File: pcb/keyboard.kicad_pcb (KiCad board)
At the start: 2 copper layers, 72.2 x 98 mm, 23 parts, among them SW1 SW_Push, SW2 SW_Push, SW3 RotaryEncoder_Switch, SW3 SW_Push, SW4 SW_Push, SW5 SW_Push, SW6 SW_Push, SW7 SW_Push, SW8 SW_Push, SW9 SW_Push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

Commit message: delete the current pcb situation - too many changes were made to the schem
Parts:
- removed D1, D2, D3, D4, D5, D6, D7, D8, D9: 1N4148, Diode_THT:D_DO-35_SOD27_P7.62mm_Horizontal
- removed D10, D11: SK6812MINI-E, footprints:SK6812MINI-E_fixed
- removed SW1, SW2, SW3, SW4, SW5, SW6, SW7, SW8, SW9: SW_Push, Button_Switch_Keyboard:SW_Cherry_MX_1.00u_PCB
- removed SW3: RotaryEncoder_Switch, Rotary_Encoder:RotaryEncoder_Alps_EC11E-Switch_Vertical_H20mm
- removed U1: MOUDLE-SEEEDUINO-XIAO, footprints:XIAO-Generic-Hybrid-14P-2.54-21X17.8MM
- removed U2: ER_OLEDM0.91_1x-I2C, Display:ER_OLEDM0.91_1x-I2C
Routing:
- net Row 2: track 154.9 -> 0.00 mm
- net Row 1: track 133.4 -> 0.00 mm
- net Row 0: track 113.0 -> 0.00 mm
- net Column 2: track 104.2 -> 0.00 mm
- net GND: track 96.8 -> 0.00 mm, vias 1 -> 0
- net Column 1: track 87.1 -> 0.00 mm
- net Column 0: track 81.6 -> 0.00 mm
- net VCC: track 43.9 -> 0.00 mm
- net ROT A: track 26.5 -> 0.00 mm
- net ROT B: track 25.5 -> 0.00 mm
- net SCL: track 24.5 -> 0.00 mm
- net SDA: track 24.5 -> 0.00 mm
- net (no net): track 22.6 -> 0.00 mm
- net Net-(D7-A): track 5.95 -> 0.00 mm
- net Net-(D4-A): track 5.91 -> 0.00 mm
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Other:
- board outline removed

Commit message: align switches, board and screen on the pcb
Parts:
- added D1: 1N4148, Diode_THT:D_DO-35_SOD27_P7.62mm_Horizontal, F.Cu at (117.3, 93.5)
- added D10: SK6812MINI-E, footprints:SK6812MINI-E_fixed, F.Cu at (175.5, 70.5)
- added D11: SK6812MINI-E, footprints:SK6812MINI-E_fixed, F.Cu at (216.0, 70.5)
- added D2: 1N4148, Diode_THT:D_DO-35_SOD27_P7.62mm_Horizontal, F.Cu at (117.3, 97.0)
- added D3: 1N4148, Diode_THT:D_DO-35_SOD27_P7.62mm_Horizontal, F.Cu at (117.3, 100.5)
- added D4: 1N4148, Diode_THT:D_DO-35_SOD27_P7.62mm_Horizontal, F.Cu at (117.3, 104.1)
- added D5: 1N4148, Diode_THT:D_DO-35_SOD27_P7.62mm_Horizontal, F.Cu at (117.3, 107.7)
- added D6: 1N4148, Diode_THT:D_DO-35_SOD27_P7.62mm_Horizontal, F.Cu at (117.3, 111.2)
- added D7: 1N4148, Diode_THT:D_DO-35_SOD27_P7.62mm_Horizontal, F.Cu at (117.3, 114.8)
- added D8: 1N4148, Diode_THT:D_DO-35_SOD27_P7.62mm_Horizontal, F.Cu at (117.3, 118.3)
- added D9: 1N4148, Diode_THT:D_DO-35_SOD27_P7.62mm_Horizontal, F.Cu at (117.3, 121.8)
- added SW1: SW_Push, Button_Switch_Keyboard:SW_Cherry_MX_1.00u_PCB, F.Cu at (178.3, 77.7)
- added SW2: SW_Push, Button_Switch_Keyboard:SW_Cherry_MX_1.00u_PCB, F.Cu at (198.0, 77.7)
- added SW3: RotaryEncoder_Switch, Rotary_Encoder:RotaryEncoder_Alps_EC11E-Switch_Vertical_H20mm, F.Cu at (208.2, 79.8)
- added SW4: SW_Push, Button_Switch_Keyboard:SW_Cherry_MX_1.00u_PCB, F.Cu at (178.3, 97.4)
- added SW5: SW_Push, Button_Switch_Keyboard:SW_Cherry_MX_1.00u_PCB, F.Cu at (198.0, 97.4)
- added SW6: SW_Push, Button_Switch_Keyboard:SW_Cherry_MX_1.00u_PCB, F.Cu at (217.7, 97.4)
- added SW7: SW_Push, Button_Switch_Keyboard:SW_Cherry_MX_1.00u_PCB, F.Cu at (178.3, 117.1)
- added SW8: SW_Push, Button_Switch_Keyboard:SW_Cherry_MX_1.00u_PCB, F.Cu at (217.7, 117.1)
- added SW9: SW_Push, Button_Switch_Keyboard:SW_Cherry_MX_1.00u_PCB, F.Cu at (198.0, 117.1)
- added U1: MODULE-SEEEDUINO-XIAO-RP2040, footprints:XIAO-Generic-Hybrid-14P-2.54-21X17.8MM, F.Cu at (175.4, 56.2)
- added U2: ER_OLEDM0.91_1x-I2C, Display:ER_OLEDM0.91_1x-I2C, F.Cu at (189.5, 59.3)
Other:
- board outline added: 70 x 95 mm

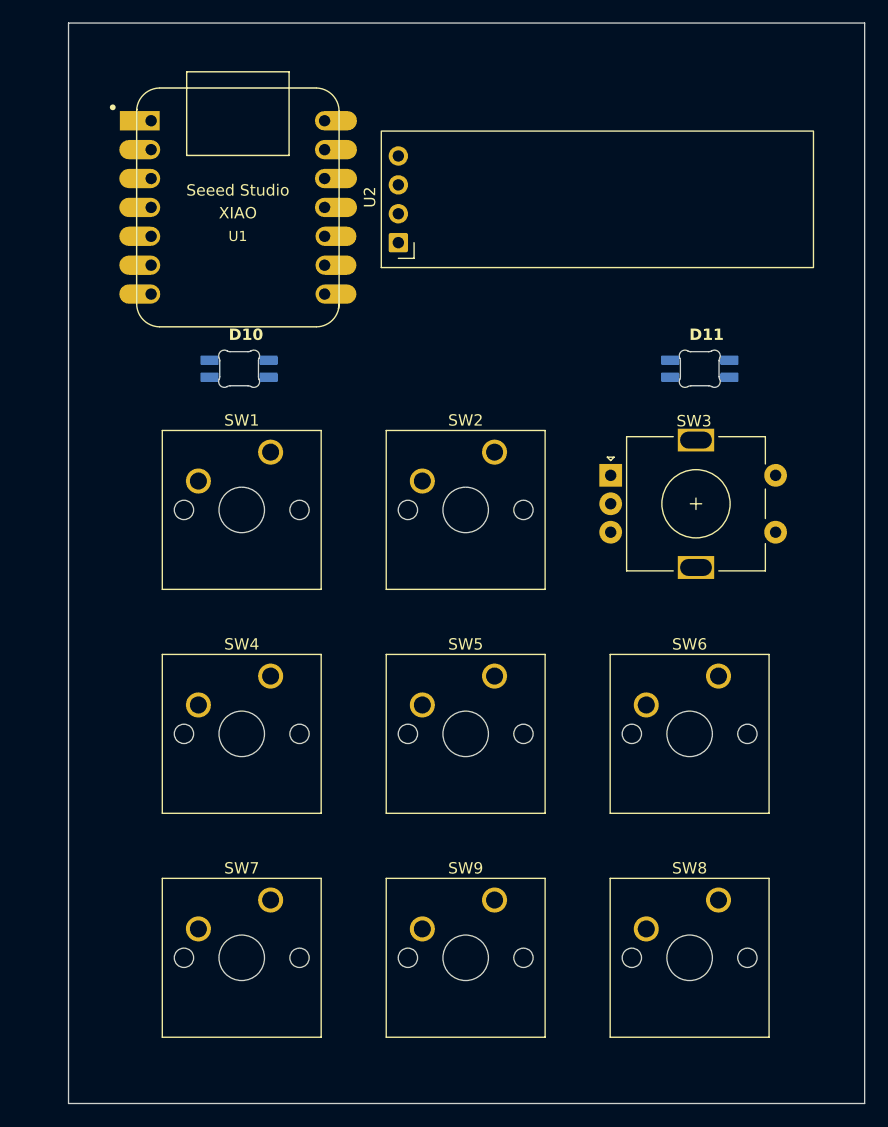
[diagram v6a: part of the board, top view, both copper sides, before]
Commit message: make the board smaller, add third rgb
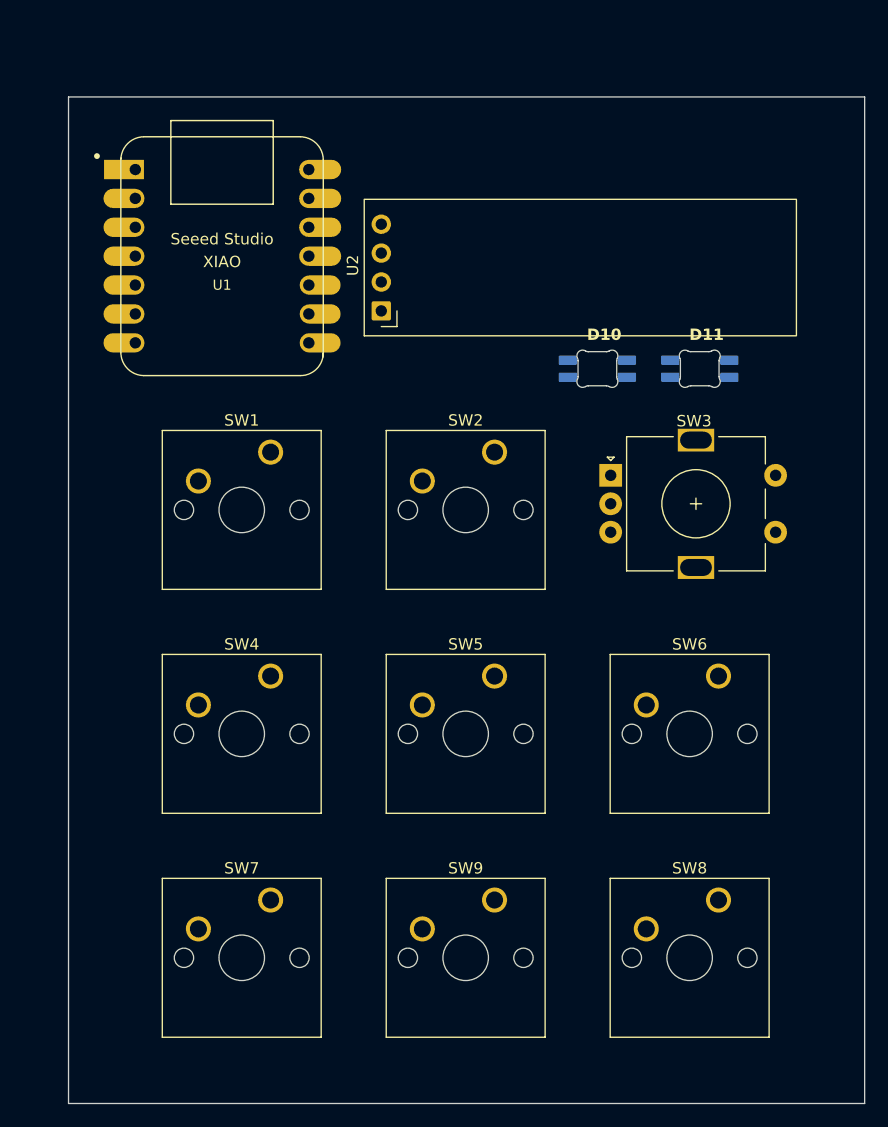
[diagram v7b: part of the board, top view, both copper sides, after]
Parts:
- moved D10 31.5 mm to (207.0, 70.5)
- moved U2 6.18 mm to (188.0, 65.3)
- moved U1 4.51 mm to (174.0, 60.5)
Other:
- board size 70 x 95 mm -> 70 x 88.5 mm
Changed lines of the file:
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@@
 	(footprint "footprints:SK6812MINI-E_fixed"
 		(layer "F.Cu")
-		(at 175.5 70.5)
+		(at 207 70.5)
 		(descr "Add-on for regular MX-footprints with SK6812 MINI-E")
 		(tags "cherry MX SK6812 Mini-E rearmount rear mount led rgb backlight")
@@
 	(footprint "Display:ER_OLEDM0.91_1x-I2C"
 		(layer "F.Cu")
-		(at 189.5 59.31 90)
+		(at 188 65.31 90)
 		(descr "SSD1306 OLED module, 0.91 inch, 128x32, I2C (https://www.buydisplay.com/download/manual/ER-OLEDM0.91-1_Datasheet.pdf)")
 		(tags "EastRising")
@@
 	(footprint "footprints:XIAO-Generic-Hybrid-14P-2.54-21X17.8MM"
 		(layer "F.Cu")
-		(at 175.3895 56.212015)
+		(at 174 60.5)
 		(property "Reference" "U1"
 			(at 0 2.54 0)
@@
 	)
 	(gr_rect
-		(start 160.5 40)
+		(start 160.5 46.5)
 		(end 230.5 135)
 		(stroke

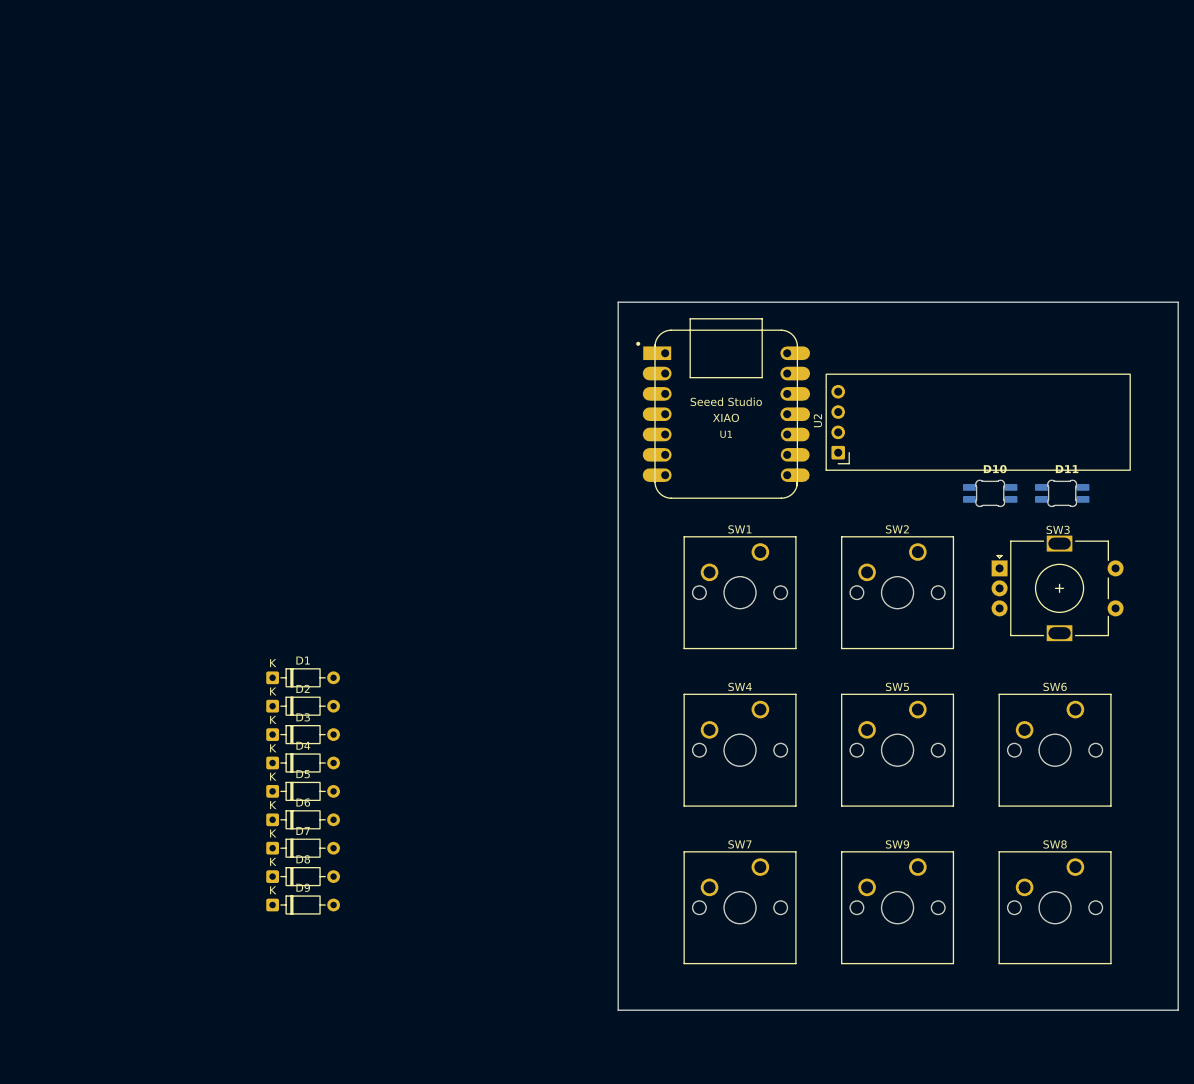
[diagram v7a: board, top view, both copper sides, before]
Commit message: align diodes
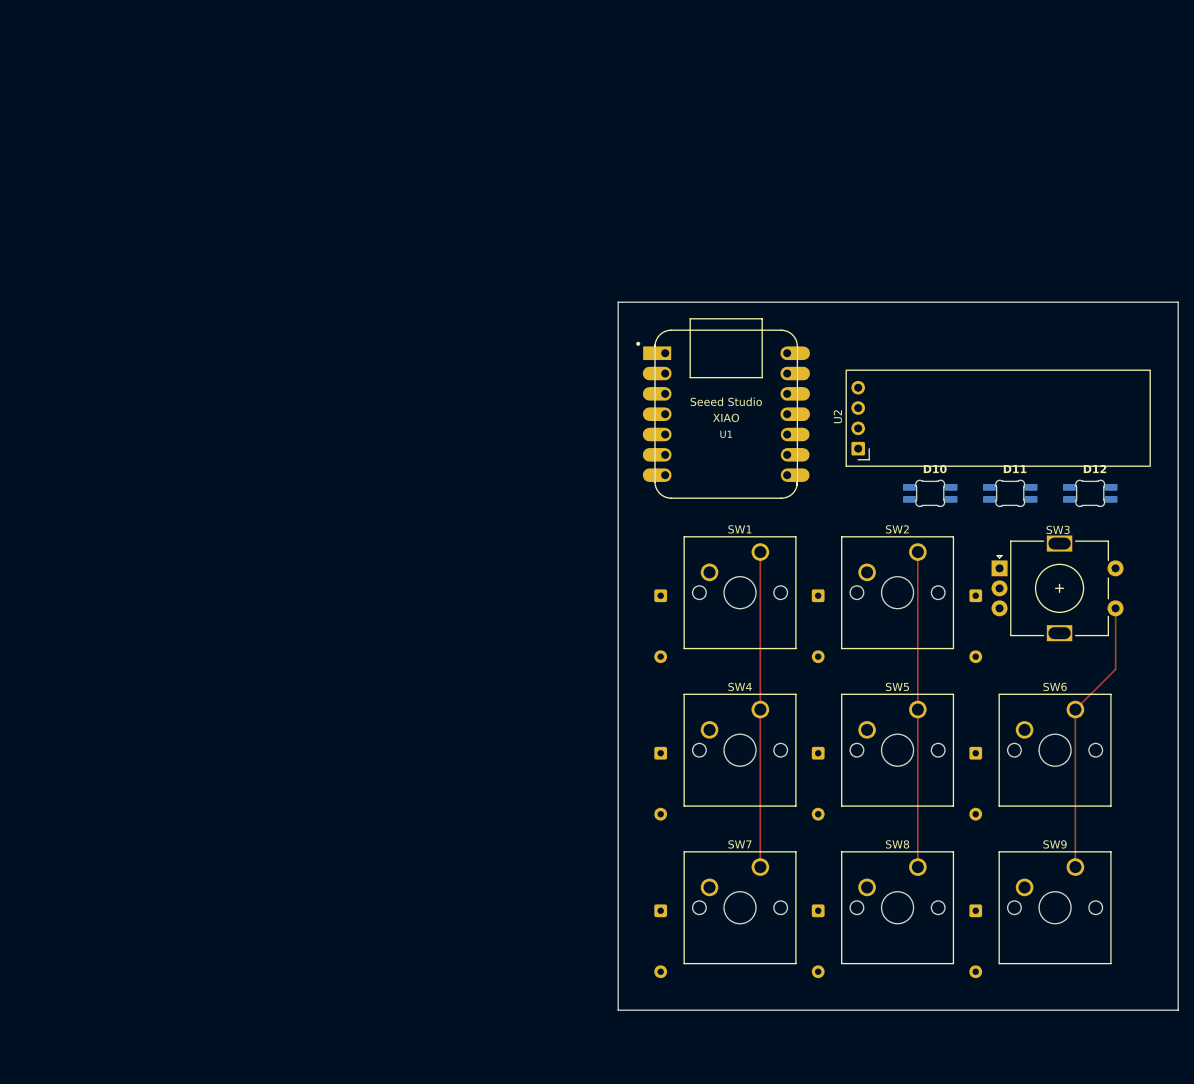
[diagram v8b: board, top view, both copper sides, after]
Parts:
- added D12: SK6812MINI-E, footprints:SK6812MINI-E_fixed, F.Cu at (219.5, 70.5)
- D1, D2, D3, D4, D5, D6, D7, D8, D9: moved to B.Cu
- moved D3 89.6 mm to (205.2, 83.2), turned to -90 degrees
- moved D6 88.3 mm to (205.2, 102.9), turned to -90 degrees
- moved D9 87.9 mm to (205.2, 122.6), turned to -90 degrees
- moved D2 69.6 mm to (185.5, 83.2), turned to -90 degrees
- moved D5 68.4 mm to (185.5, 102.9), turned to -90 degrees
- moved D8 68.3 mm to (185.5, 122.6), turned to -90 degrees
- moved D1 49.6 mm to (165.8, 83.2), turned to -90 degrees
- moved D7 49.1 mm to (165.8, 122.6), turned to -90 degrees
- moved D4 48.5 mm to (165.8, 102.9), turned to -90 degrees
- moved SW8 19.7 mm to (198.0, 117.1)
- moved SW9 19.7 mm to (217.7, 117.1)
- moved D10 7.50 mm to (199.5, 70.5)
- moved D11 6.50 mm to (209.5, 70.5)
- moved U2 2.55 mm to (190.5, 64.8)
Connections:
- D11 pad 4: unconnected-(D11-DOUT-Pad4) -> Net-(D11-DOUT)
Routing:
- net Column 1: track 0.00 -> 39.4 mm
- net Column 0: track 0.00 -> 39.4 mm
- net Column 2: track 0.00 -> 34.4 mm
